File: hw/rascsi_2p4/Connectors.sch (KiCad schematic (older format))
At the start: 2 parts, among them J3 Conn_02x25_Odd_Even, J9 Conn_02x25_Odd_Even

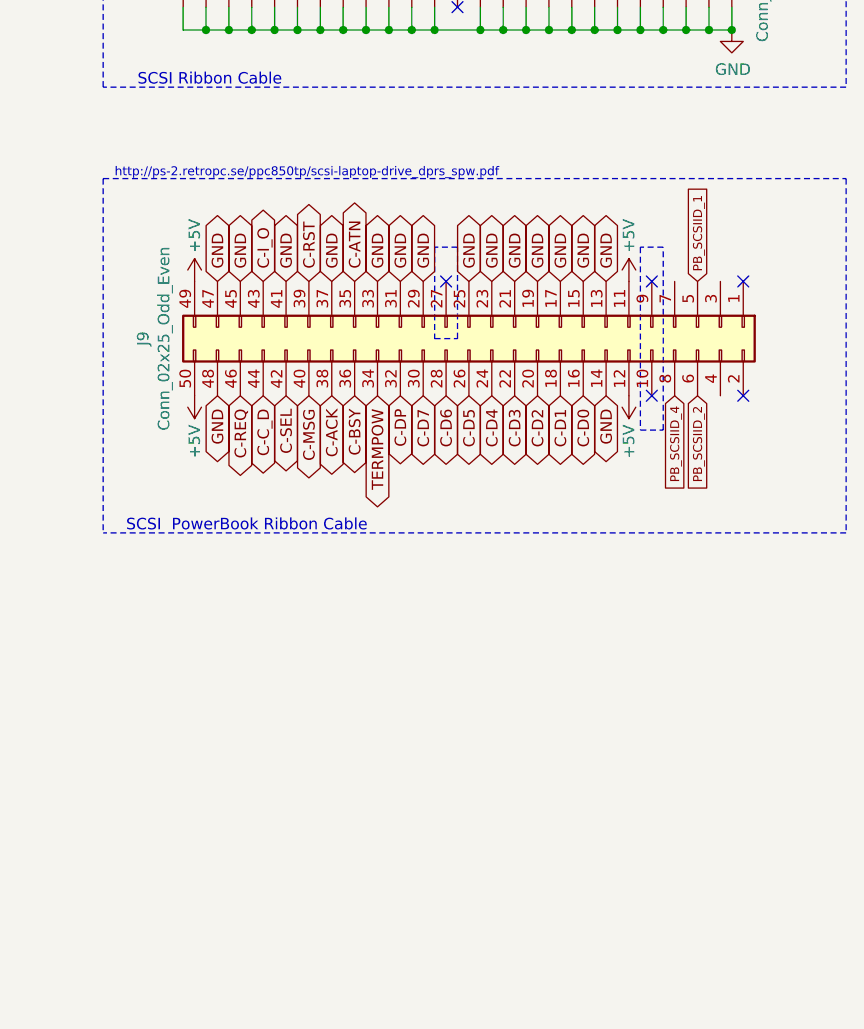
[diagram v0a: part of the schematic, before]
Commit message: Clean up silkscreen and fix DRC issues
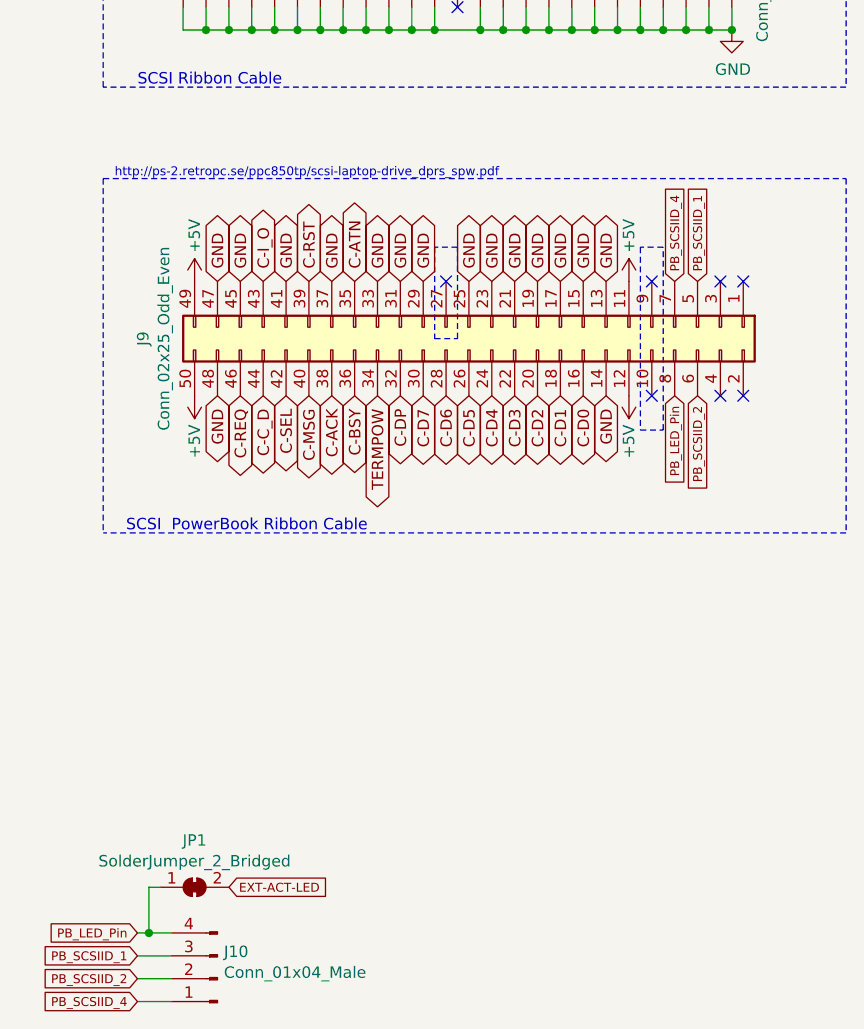
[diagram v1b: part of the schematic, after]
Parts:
- added J10: Conn_01x04_Male, Connector_PinHeader_1.00mm:PinHeader_1x04_P1.00mm_Vertical, symbol Connector:Conn_01x04_Male
- added JP1: SolderJumper_2_Bridged, Jumper:SolderJumper-2_P1.3mm_Bridged_Pad1.0x1.5mm, symbol Jumper:SolderJumper_2_Bridged
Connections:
- net PB_SCSIID_1: now also J10.3 (Pin_3)
- net PB_SCSIID_2: now also J10.2 (Pin_2)
- net PB_SCSIID_4: now also J9.7 (Pin_7), J10.1 (Pin_1); no longer J9.8 (Pin_8)
- new net EXT-ACT-LED: JP1.2 (B)
- new net PB_LED_Pin: J10.4 (Pin_4), J9.8 (Pin_8), JP1.1 (A)
- no-connect marks 7 -> 9
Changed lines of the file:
@@
 Text GLabel 4000 3600 3    39   Input ~ 0
 PB_SCSIID_2
-Text GLabel 3900 3600 3    39   Input ~ 0
+Text GLabel 3900 3100 1    39   Input ~ 0
 PB_SCSIID_4
 NoConn ~ 3800 3100
@@
 Text Notes 1450 2650 0    39   ~ 0
 http://ps-2.retropc.se/ppc850tp/scsi-laptop-drive_dprs_spw.pdf
+Text GLabel 3900 3600 3    39   Input ~ 0
+PB_LED_Pin
+NoConn ~ 4100 3100
+NoConn ~ 4100 3600
+Text GLabel 1550 6050 0    39   Input ~ 0
+PB_SCSIID_1
+Text GLabel 1550 6250 0    39   Input ~ 0
+PB_SCSIID_4
+Text GLabel 1550 6150 0    39   Input ~ 0
+PB_SCSIID_2
+Text GLabel 1550 5950 0    39   Input ~ 0
+PB_LED_Pin
+$Comp
+L Jumper:SolderJumper_2_Bridged JP1
+U 1 1 5FF168EB
+P 1800 5750
+F 0 "JP1" H 1800 5955 50  0000 C CNN
+F 1 "SolderJumper_2_Bridged" H 1800 5864 50  0000 C CNN
+F 2 "Jumper:SolderJumper-2_P1.3mm_Bridged_Pad1.0x1.5mm" H 1800 5750 50  0001 C CNN
+F 3 "~" H 1800 5750 50  0001 C CNN
+	1    1800 5750
+	1    0    0    -1
+$EndComp
+Wire Wire Line
+	1550 6250 1700 6250
+Wire Wire Line
+	1550 6150 1700 6150
+Wire Wire Line
+	1550 6050 1700 6050
+Wire Wire Line
+	1550 5950 1600 5950
+Wire Wire Line
+	1650 5750 1600 5750
+Wire Wire Line
+	1600 5750 1600 5950
+Connection ~ 1600 5950
+Wire Wire Line
+	1600 5950 1700 5950
+Text GLabel 1950 5750 2    39   Input ~ 0
+EXT-ACT-LED
+$Comp
+L Connector:Conn_01x04_Male J10
+U 1 1 5FF34865
+P 1900 6150
+F 0 "J10" H 1872 6032 50  0000 R CNN
+F 1 "Conn_01x04_Male" H 1872 6123 50  0000 R CNN
+F 2 "Connector_PinHeader_1.00mm:PinHeader_1x04_P1.00mm_Vertical" H 1900 6150 50  0001 C CNN
+F 3 "~" H 1900 6150 50  0001 C CNN
+	1    1900 6150
+	-1   0    0    1
+$EndComp
 $EndSCHEMATC

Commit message: additional cleanup. Made Pin 1 of the PB connector square
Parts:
- J10: footprint Connector_PinHeader_1.00mm:PinHeader_1x04_P1.00mm_Vertical -> Connector_PinHeader_2.00mm:PinHeader_1x04_P2.00mm_Vertical
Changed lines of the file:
@@
 F 0 "J10" H 1872 6032 50  0000 R CNN
 F 1 "Conn_01x04_Male" H 1872 6123 50  0000 R CNN
-F 2 "Connector_PinHeader_1.00mm:PinHeader_1x04_P1.00mm_Vertical" H 1900 6150 50  0001 C CNN
+F 2 "Connector_PinHeader_2.00mm:PinHeader_1x04_P2.00mm_Vertical" H 1900 6150 50  0001 C CNN
 F 3 "~" H 1900 6150 50  0001 C CNN
 	1    1900 6150

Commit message: minor tweaks
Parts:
- J9: Description Header 50 0.100\"(2.54mm) 2 2.54MM IDC Connectors RoHS -> CUT DOWN TO 50 PIN - Pin Header 80 2 right-angle，90degrees 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; LCSC C30006 -> C3407; Manufacturer_Part_Number C30006 -> C3407
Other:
- note added: "Remove pins 9, 10 and 27"
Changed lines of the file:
@@
 F 1 "Conn_02x25_Odd_Even" H 3050 1966 50  0000 C CNN
 F 2 "Connector_PinHeader_2.00mm:PinHeader_2x25_P2.00mm_Horizontal" H 3000 3300 50  0001 C CNN
-F 3 "https://datasheet.lcsc.com/szlcsc/1810221914_BOOMELE-Boom-Precision-Elec-C30006_C30006.pdf" H 3000 3300 50  0001 C CNN
-F 4 "C30006" H 3000 3300 50  0001 C CNN "LCSC"
-F 5 "Header 50 0.100\"(2.54mm) 2 2.54MM IDC Connectors RoHS" H 3000 3300 50  0001 C CNN "Description"
+F 3 "https://datasheet.lcsc.com/szlcsc/1811151534_BOOMELE-Boom-Precision-Elec-C3407_C3407.pdf" H 3000 3300 50  0001 C CNN
+F 4 "C3407" H 3000 3300 50  0001 C CNN "LCSC"
+F 5 "CUT DOWN TO 50 PIN - Pin Header 80 2 right-angle，90degrees 2.00mm Through Hole Pin Header" H 3000 3300 50  0001 C CNN "Description"
 F 6 "BOOMELE(Boom Precision Elec)" H 3000 3300 50  0001 C CNN "Manufacturer_Name"
-F 7 "C30006" H 3000 3300 50  0001 C CNN "Manufacturer_Part_Number"
+F 7 "C3407" H 3000 3300 50  0001 C CNN "Manufacturer_Part_Number"
 F 8 "" H 3000 3300 50  0001 C CNN "Mouser Part Number"
 F 9 "" H 3000 3300 50  0001 C CNN "Mouser Price/Stock"
@@
 	-1   0    0    1
 $EndComp
+Text Notes 2900 4150 0    79   ~ 16
+Remove pins 9, 10 and 27
 $EndSCHEMATC

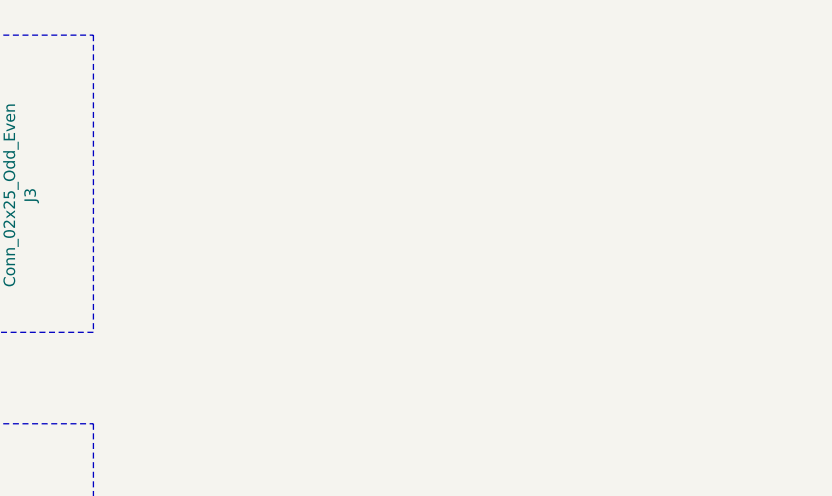
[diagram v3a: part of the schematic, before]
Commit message: Added optional floppy power connector. As-ordered version 2.4a
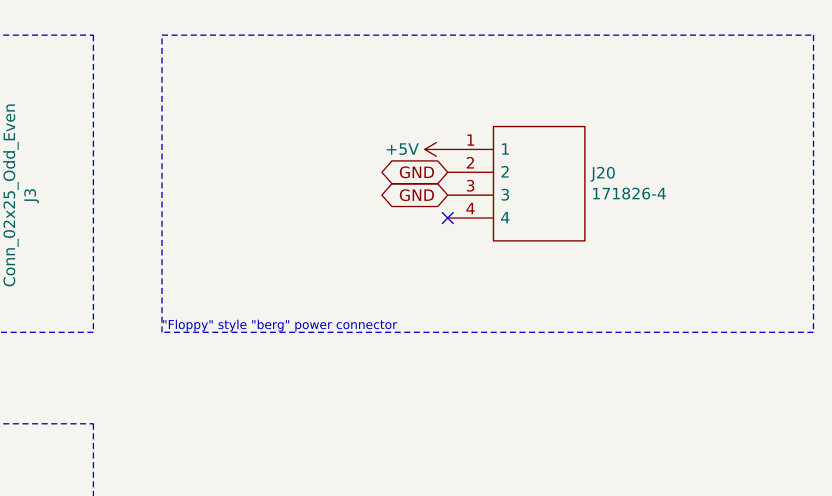
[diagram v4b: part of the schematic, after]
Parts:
- added J20: 171826-4, SHDRRA4W69P0X250_1X4_1000X1350X670P, symbol SamacSys_Parts:171826-4
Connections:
- net +5V: now also J20.1
- net GND: now also J20.2, J20.3
- no-connect marks 9 -> 10
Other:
- note added: ""Floppy" style "berg" power connector"
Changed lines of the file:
@@
 Text Notes 2900 4150 0    79   ~ 16
 Remove pins 9, 10 and 27
+$Comp
+L SamacSys_Parts:171826-4 J20
+U 1 1 607408EC
+P 6200 1450
+F 0 "J20" H 6828 1346 50  0000 L CNN
+F 1 "171826-4" H 6828 1255 50  0000 L CNN
+F 2 "SHDRRA4W69P0X250_1X4_1000X1350X670P" H 6850 1550 50  0001 L CNN
+F 3 "https://componentsearchengine.com/Datasheets/2/171826-4.pdf" H 6850 1450 50  0001 L CNN
+F 4 "Headers & Wire Housings 4P HDR R/A" H 6850 1350 50  0001 L CNN "Description"
+F 5 "6.7" H 6850 1250 50  0001 L CNN "Height"
+F 6 "571-1718264" H 6850 1150 50  0001 L CNN "Mouser Part Number"
+F 7 "https://www.mouser.co.uk/ProductDetail/TE-Connectivity/171826-4/?qs=4hg9R9g9MDt3qYFe2l2pbA%3D%3D" H 6850 1050 50  0001 L CNN "Mouser Price/Stock"
+F 8 "TE Connectivity" H 6850 950 50  0001 L CNN "Manufacturer_Name"
+F 9 "171826-4" H 6850 850 50  0001 L CNN "Manufacturer_Part_Number"
+	1    6200 1450
+	1    0    0    -1
+$EndComp
+Wire Notes Line
+	4950 950  7800 950
+Wire Notes Line
+	7800 950  7800 2250
+Wire Notes Line
+	7800 2250 4950 2250
+Wire Notes Line
+	4950 2250 4950 950
+Text Notes 4950 2250 0    39   ~ 0
+"Floppy" style "berg" power connector
+Text GLabel 6200 1550 0    50   BiDi ~ 0
+GND
+$Comp
+L power:+5V #PWR053
+U 1 1 607432AF
+P 6200 1450
+F 0 "#PWR053" H 6200 1300 50  0001 C CNN
+F 1 "+5V" V 6200 1650 50  0000 C CNN
+F 2 "" H 6200 1450 50  0001 C CNN
+F 3 "" H 6200 1450 50  0001 C CNN
+	1    6200 1450
+	0    -1   -1   0
+$EndComp
+Text GLabel 6200 1650 0    50   BiDi ~ 0
+GND
+NoConn ~ 6200 1750
 $EndSCHEMATC
